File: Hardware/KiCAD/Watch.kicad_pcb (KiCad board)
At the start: 2 copper layers, 36 x 36 mm, 26 parts, among them IC102 BQ32002D, U101 ATSAM4LS2AA-AU

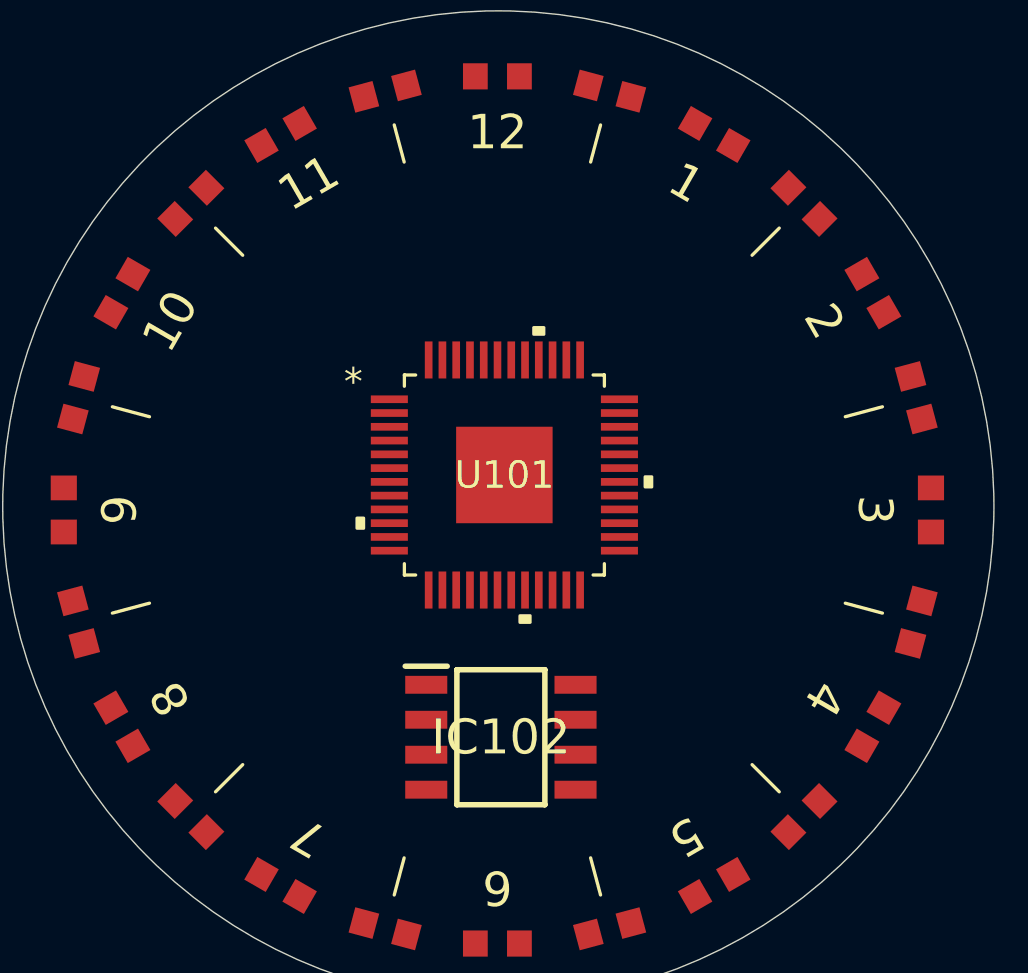
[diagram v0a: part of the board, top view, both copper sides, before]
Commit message: Light driver schematic layout complete
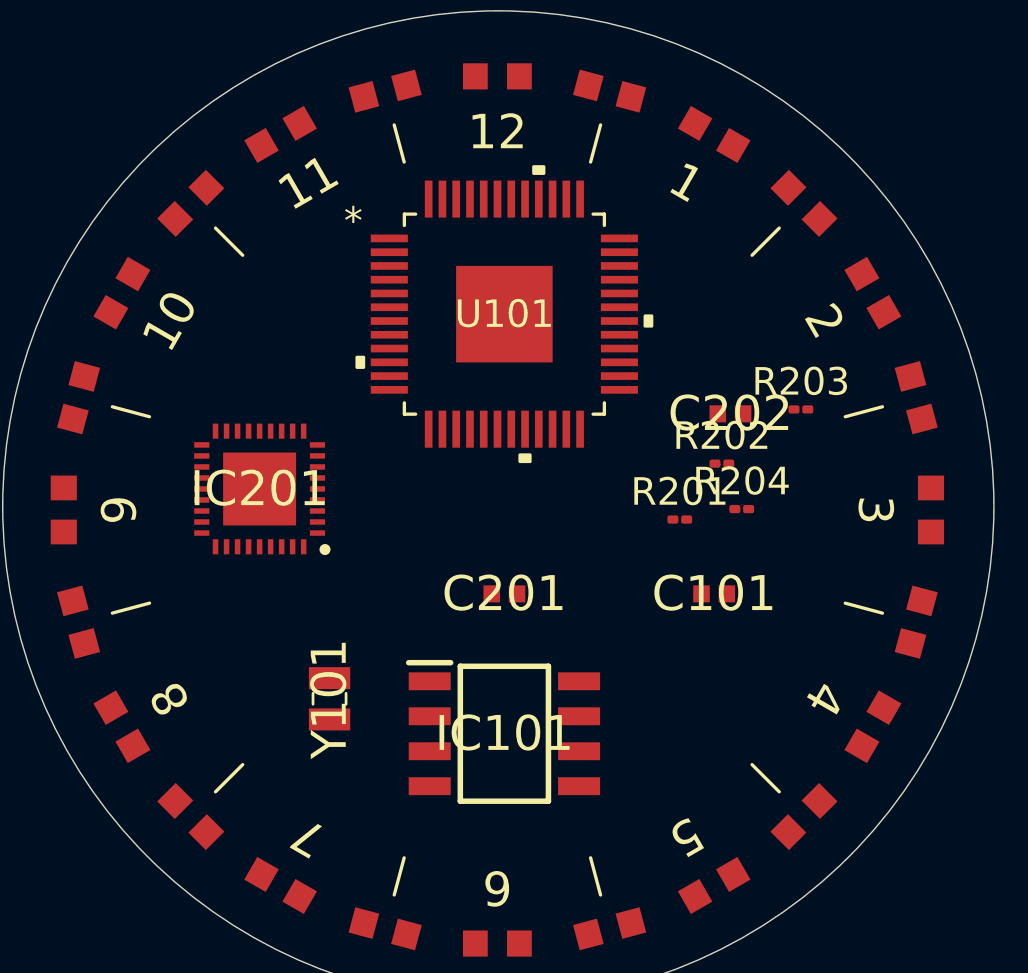
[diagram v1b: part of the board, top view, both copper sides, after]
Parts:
- removed IC102: BQ32002D, SamacSys_Parts:SOIC127P600X175-8N
- added C101: ?uF, SamacSys_Parts:CAPC1005X55N, F.Cu at (153.7, 91.4)
- added C201: 0.1uF, SamacSys_Parts:CAPC1005X55N, F.Cu at (146.1, 91.4)
- added C202: 1uF, SamacSys_Parts:CAPC1005X55N, F.Cu at (154.3, 84.9)
- added IC101: PT7C4563BQ1WEX, SamacSys_Parts:SOIC127P600X175-8N, F.Cu at (146.1, 96.5)
- added IC201: IS31FL3235A-QFLS2-TR, SamacSys_Parts:QFN40P400X400X80-37N, F.Cu at (137.2, 87.6)
- added R201: 4.7k, Resistor_SMD:R_01005_0402Metric, F.Cu at (152.4, 88.7)
- added R202: 4.7k, Resistor_SMD:R_01005_0402Metric, F.Cu at (153.9, 86.7)
- added R203: 3.3k, Resistor_SMD:R_01005_0402Metric, F.Cu at (156.8, 84.7)
- added R204: 100k, Resistor_SMD:R_01005_0402Metric, F.Cu at (154.7, 88.4)
- added Y101: CM8V-T1A-32.768kHz-4pF-20PPM-TA-QC_T3, SamacSys_Parts:CM8V32768TA020125, F.Cu at (139.7, 95.2)
- moved U101 5.84 mm to (146.1, 81.3)
- renumbered LED201 to LED202, LED201 to LED203, LED201 to LED204, LED201 to LED205, LED201 to LED206, LED201 to LED207, LED201 to LED208, LED201 to LED209, LED201 to LED210, LED201 to LED211, LED201 to LED212, LED201 to LED213, LED201 to LED214, LED201 to LED215, LED201 to LED216, LED201 to LED217, LED201 to LED218, LED201 to LED219, LED201 to LED220, LED201 to LED221, LED201 to LED222, LED201 to LED223, LED201 to LED224
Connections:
- net Net-(LED201-Pad2) renamed +3V3
- LED201 pad 1: Net-(LED201-Pad1) -> /leds/OUT1
- LED202 pad 1: Net-(LED201-Pad1) -> /leds/OUT2
- LED203 pad 1: Net-(LED201-Pad1) -> /leds/OUT3
- LED204 pad 1: Net-(LED201-Pad1) -> /leds/OUT4
- LED205 pad 1: Net-(LED201-Pad1) -> /leds/OUT5
- LED206 pad 1: Net-(LED201-Pad1) -> /leds/OUT6
- LED207 pad 1: Net-(LED201-Pad1) -> /leds/OUT7
- LED208 pad 1: Net-(LED201-Pad1) -> /leds/OUT8
- LED209 pad 1: Net-(LED201-Pad1) -> /leds/OUT9
- LED210 pad 1: Net-(LED201-Pad1) -> /leds/OUT10
- LED211 pad 1: Net-(LED201-Pad1) -> /leds/OUT12
- LED212 pad 1: Net-(LED201-Pad1) -> /leds/OUT13
- LED213 pad 1: Net-(LED201-Pad1) -> /leds/OUT14
- LED214 pad 1: Net-(LED201-Pad1) -> /leds/OUT15
- LED215 pad 1: Net-(LED201-Pad1) -> /leds/OUT16
- LED216 pad 1: Net-(LED201-Pad1) -> /leds/OUT17
- LED217 pad 1: Net-(LED201-Pad1) -> /leds/OUT18
- LED218 pad 1: Net-(LED201-Pad1) -> /leds/OUT19
- LED219 pad 1: Net-(LED201-Pad1) -> /leds/OUT20
- LED220 pad 1: Net-(LED201-Pad1) -> /leds/OUT21
- LED221 pad 1: Net-(LED201-Pad1) -> /leds/OUT21
- LED222 pad 1: Net-(LED201-Pad1) -> /leds/OUT22
- LED223 pad 1: Net-(LED201-Pad1) -> /leds/OUT23
- LED224 pad 1: Net-(LED201-Pad1) -> /leds/OUT24

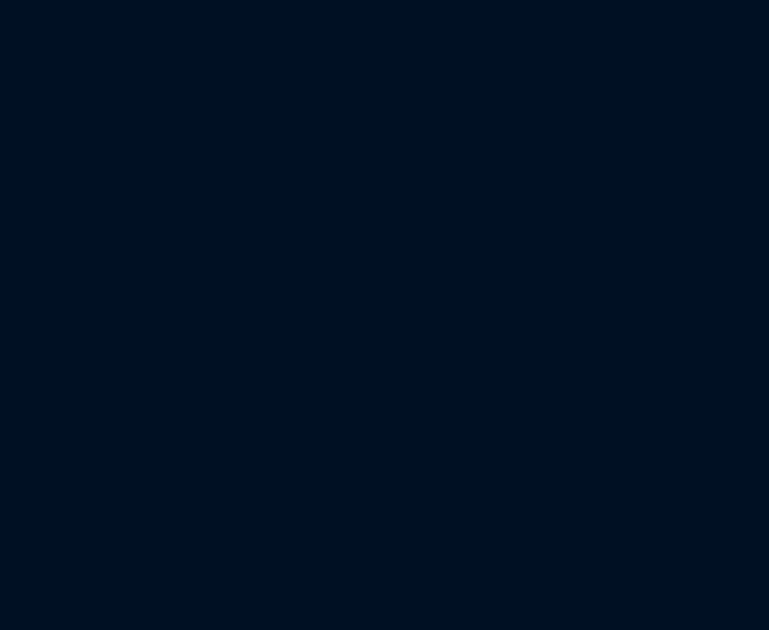
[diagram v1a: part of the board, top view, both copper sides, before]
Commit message: LTSpice zener diode tests. Watch HW now has lipo charger IC and RGB LED for status monitoring
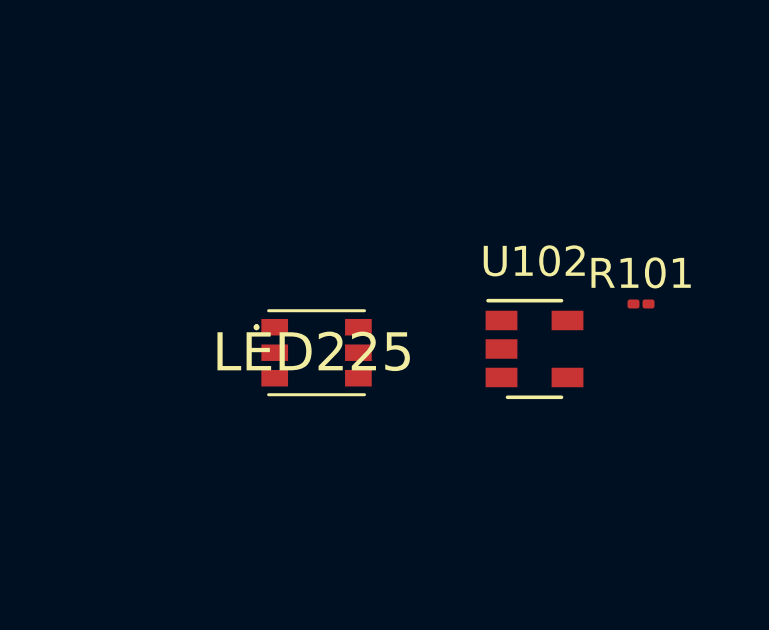
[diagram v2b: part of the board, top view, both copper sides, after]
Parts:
- added LED225: RGB LED, SamacSys_Parts:150352M173300, F.Cu at (181.6, 91.4)
- added R101: 10k, Resistor_SMD:R_01005_0402Metric, F.Cu at (192.4, 89.8)
- added U102: MCP73831-2-OT, Package_TO_SOT_SMD:SOT-23-5, F.Cu at (188.9, 91.3)

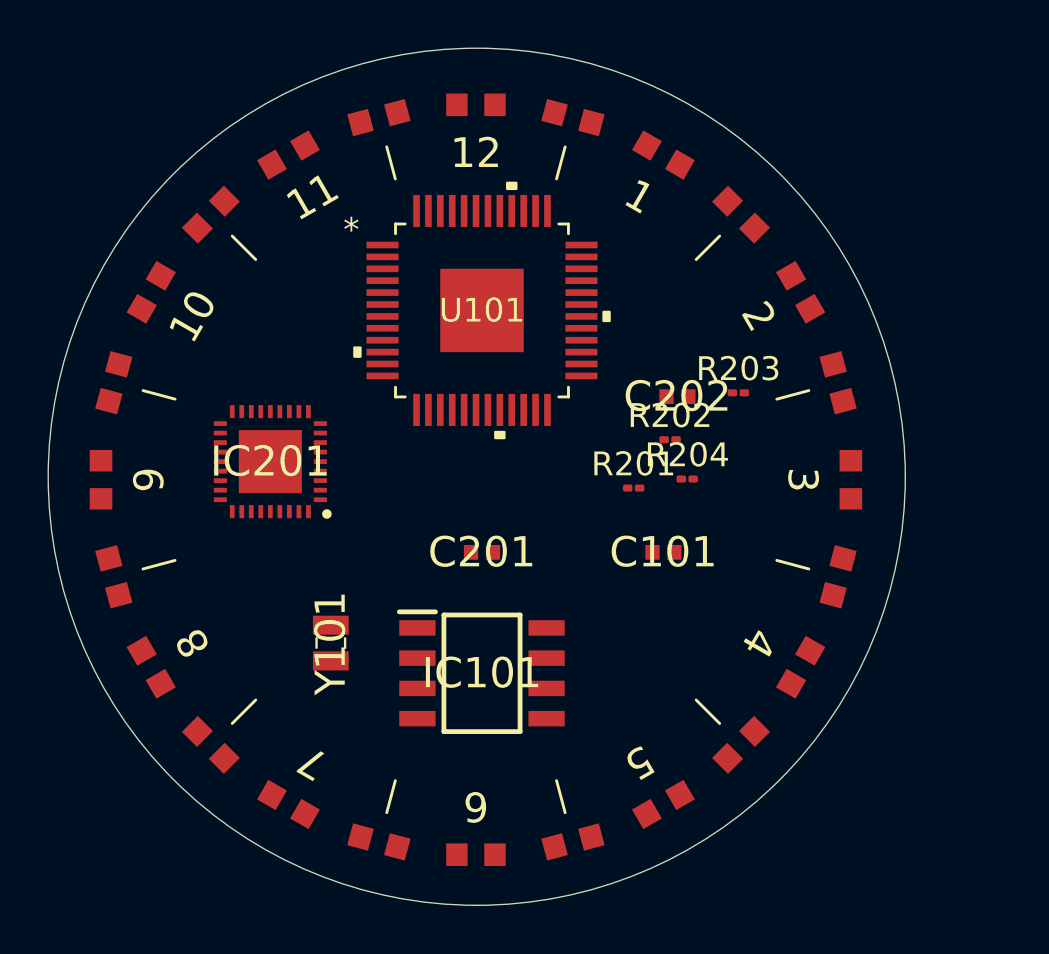
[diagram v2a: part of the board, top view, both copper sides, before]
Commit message: Hardware mounting aligned. Dimensions set.
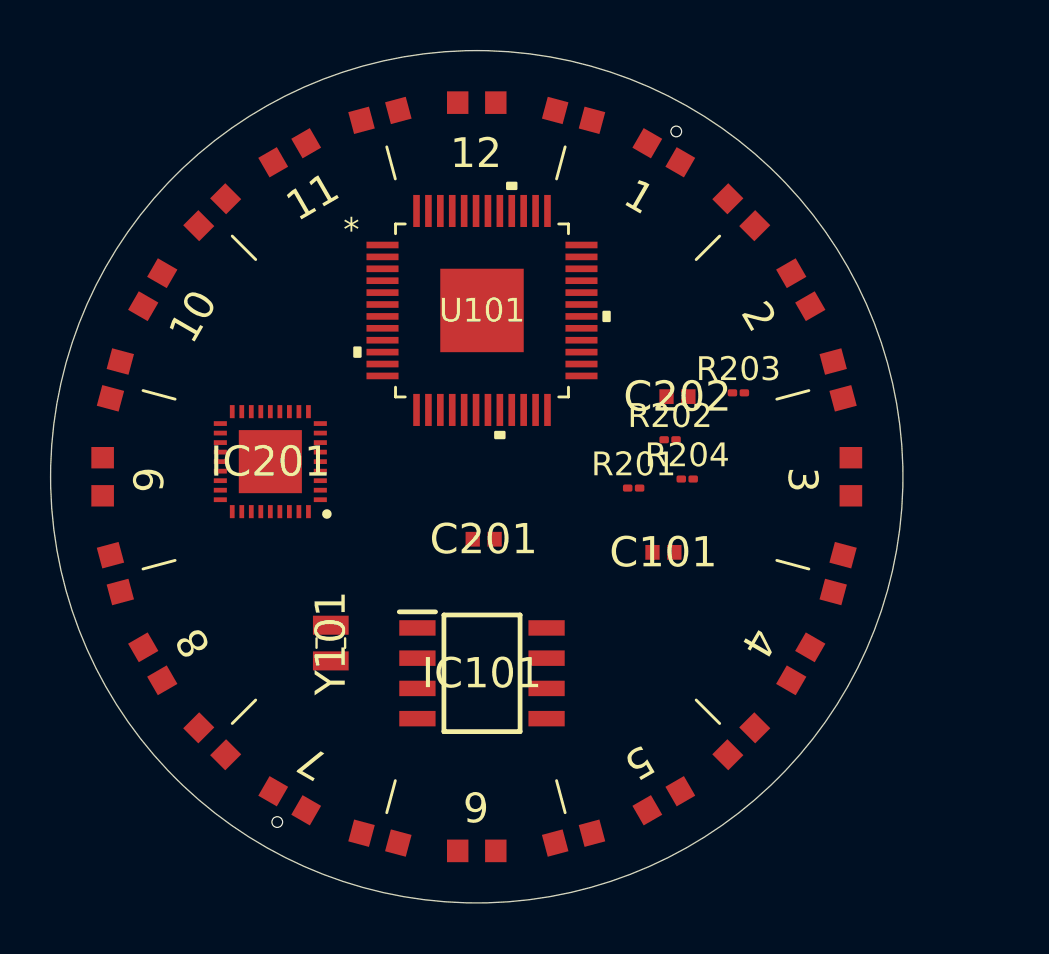
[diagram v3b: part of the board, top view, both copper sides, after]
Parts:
- moved LED219 4.24 mm to (130.7, 84.2), turned to 255 degrees
- moved LED220 4.24 mm to (132.2, 80.4), turned to 240 degrees
- moved LED218 4.23 mm to (130.1, 88.3), turned to 270 degrees
- moved LED221 4.23 mm to (134.7, 77.2), turned to 225 degrees
- moved LED217 4.21 mm to (130.7, 92.3), turned to 285 degrees
- moved LED222 4.21 mm to (138.0, 74.7), turned to 210 degrees
- moved LED216 4.19 mm to (132.2, 96.1), turned to 300 degrees
- moved LED223 4.19 mm to (141.8, 73.1), turned to 195 degrees
- moved LED215 4.16 mm to (134.7, 99.4), turned to 315 degrees
- moved LED224 4.16 mm to (145.8, 72.6), turned to 180 degrees
- moved LED214 4.13 mm to (138.0, 101.9), turned to 330 degrees
- moved LED201 4.12 mm to (149.9, 73.1), turned to 165 degrees
- moved LED213 4.09 mm to (141.8, 103.4), turned to 345 degrees
- moved LED202 4.09 mm to (153.7, 74.7), turned to 150 degrees
- moved LED212 4.06 mm to (145.8, 104.0), turned to 0 degrees
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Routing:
- net (no net): vias 0 -> 2
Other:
- board size 36 x 36 mm -> 35.8 x 35.8 mm

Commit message: Omega layout and silkscreen complete!
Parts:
- removed LED201, LED202, LED203, LED204, LED205, LED207, LED208, LED209, LED210, LED211, LED212, LED213, LED214, LED215, LED216, LED217, LED218, LED219, LED220, LED221, LED222, LED223, LED224: LTST-C191KRKT, SamacSys_Parts:LEDC1608X55N
- removed the LED206 at (161.5, 88.3)
- added G***: LOGO, Graphics:2, F.Cu at (145.8, 88.4)
- added LED206: LTST-C191KRKT, SamacSys_Parts:LEDC1608X55N, F.Cu at (159.4, 91.9)
- added LED206: LTST-C191KRKT, SamacSys_Parts:LEDC1608X55N, F.Cu at (133.7, 95.3)
- added LED206: LTST-C191KRKT, SamacSys_Parts:LEDC1608X55N, F.Cu at (132.2, 91.9)
- added LED206: LTST-C191KRKT, SamacSys_Parts:LEDC1608X55N, F.Cu at (131.8, 88.3)
- added LED206: LTST-C191KRKT, SamacSys_Parts:LEDC1608X55N, F.Cu at (132.2, 84.6)
- added LED206: LTST-C191KRKT, SamacSys_Parts:LEDC1608X55N, F.Cu at (133.7, 81.2)
- added LED206: LTST-C191KRKT, SamacSys_Parts:LEDC1608X55N, F.Cu at (135.9, 78.3)
- added LED206: LTST-C191KRKT, SamacSys_Parts:LEDC1608X55N, F.Cu at (138.8, 76.1)
- added LED206: LTST-C191KRKT, SamacSys_Parts:LEDC1608X55N, F.Cu at (142.2, 74.7)
- added LED206: LTST-C191KRKT, SamacSys_Parts:LEDC1608X55N, F.Cu at (145.8, 74.2)
- added LED206: LTST-C191KRKT, SamacSys_Parts:LEDC1608X55N, F.Cu at (149.5, 74.7)
- added LED206: LTST-C191KRKT, SamacSys_Parts:LEDC1608X55N, F.Cu at (158.0, 95.3)
- added LED206: LTST-C191KRKT, SamacSys_Parts:LEDC1608X55N, F.Cu at (152.9, 76.1)
- added LED206: LTST-C191KRKT, SamacSys_Parts:LEDC1608X55N, F.Cu at (155.8, 78.3)
- added LED206: LTST-C191KRKT, SamacSys_Parts:LEDC1608X55N, F.Cu at (158.0, 81.2)
- added LED206: LTST-C191KRKT, SamacSys_Parts:LEDC1608X55N, F.Cu at (159.4, 84.6)
- added LED206: LTST-C191KRKT, SamacSys_Parts:LEDC1608X55N, F.Cu at (159.9, 88.3)
- added LED206: LTST-C191KRKT, SamacSys_Parts:LEDC1608X55N, F.Cu at (155.8, 98.2)
- added LED206: LTST-C191KRKT, SamacSys_Parts:LEDC1608X55N, F.Cu at (152.9, 100.4)
- added LED206: LTST-C191KRKT, SamacSys_Parts:LEDC1608X55N, F.Cu at (149.5, 101.8)
- added LED206: LTST-C191KRKT, SamacSys_Parts:LEDC1608X55N, F.Cu at (145.8, 102.3)
- added LED206: LTST-C191KRKT, SamacSys_Parts:LEDC1608X55N, F.Cu at (142.2, 101.8)
- added LED206: LTST-C191KRKT, SamacSys_Parts:LEDC1608X55N, F.Cu at (138.8, 100.4)
- added LED206: LTST-C191KRKT, SamacSys_Parts:LEDC1608X55N, F.Cu at (135.9, 98.2)
- moved C201 35.6 mm to (181.2, 84.7)
- moved U102 35.5 mm to (153.4, 91.4)
- moved LED225 31.2 mm to (152.1, 81.2)
- moved C101 21.7 mm to (175.3, 89.7)
- moved C202 21.7 mm to (175.8, 83.1)
- moved R201 21.7 mm to (174.0, 87.0)
- moved R202 21.7 mm to (175.5, 84.9)
- moved R203 21.7 mm to (178.4, 83.0)
- moved R204 21.7 mm to (176.3, 86.6)
- moved IC201 15.4 mm to (152.5, 86.4)
- moved R101 12.6 mm to (180.0, 87.9)
- moved U101 12.6 mm to (145.8, 93.9)
- moved IC101 12.4 mm to (139.1, 86.2), turned to 90 degrees
- moved Y101 10.7 mm to (145.7, 86.4), turned to 180 degrees
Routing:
- net (no net): vias 2 -> 0
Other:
- board size 35.8 x 35.8 mm -> 32 x 32 mm
